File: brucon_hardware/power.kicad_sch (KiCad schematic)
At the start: 27 parts, among them J201 Conn_01x03, Q201 AO3400A, SW201 SW_SPDT, U201 TP4056, U202 MT3608, U203 HT75xx-1-SOT89

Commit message: Updated led matrix
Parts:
- renumbered C203 to C202, C204 to C203, C205 to C204, C206 to C205, C202 to C206, R209 to R201, R210 to R202, R201 to R203, R202 to R204, R204 to R205, R205 to R207, R211 to R208, R207 to R209, R208 to R210, R203 to R211
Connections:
- net VBUS: now also R201.2; no longer R201.1
- net at Q201.1 (G): now also R201.1; no longer R201.2
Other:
- moved on the sheet: R201

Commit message: Updated bom
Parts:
- C201, C203, C204: value C -> 22uF; footprint (none) -> Capacitor_SMD:C_0805_2012Metric; LCSC (none) -> C45783
- C202, C206: footprint (none) -> Capacitor_SMD:C_0805_2012Metric; LCSC (none) -> C45783
- C205: footprint (none) -> Capacitor_SMD:C_0603_1608Metric
- D201, D202: footprint (none) -> LED_SMD:LED_0805_2012Metric; LCSC (none) -> C84256
- D203: value D_Schottky -> SS54F; footprint (none) -> Diode_SMD:D_SMA; LCSC (none) -> C5359893
- J201: LCSC (none) -> C3036372
- L201: value L -> 4.7uH; footprint (none) -> Inductor_SMD:L_Sunlord_MWSA0603S; LCSC (none) -> C5307631; PNR (none) -> XR0630-4R7M
- Q201: LCSC (none) -> C20917
- R201: value R -> 10; footprint (none) -> Resistor_SMD:R_0603_1608Metric; LCSC (none) -> C22859
- R202, R203, R204: value R -> 1k; footprint (none) -> Resistor_SMD:R_0603_1608Metric; LCSC (none) -> C21190
- R205, R206, R207, R211: footprint (none) -> Resistor_SMD:R_0603_1608Metric
- R208: footprint (none) -> Resistor_SMD:R_0603_1608Metric; LCSC (none) -> C21189
- R209: value R -> 11k; footprint (none) -> Resistor_SMD:R_0603_1608Metric; LCSC (none) -> C25950
- R210: value R -> 1.5k; footprint (none) -> Resistor_SMD:R_0603_1608Metric; LCSC (none) -> C22843
- SW201: footprint (none) -> Button_Switch_SMD:SW_SPDT_PCM12; LCSC (none) -> C3036445
- U201: footprint (none) -> Package_SO:SOP-8-1EP_4.57x4.57mm_P1.27mm_EP4.57x4.45mm; LCSC (none) -> C20199357
- U202: value MT3608 -> MT3608L; LCSC (none) -> C2932326
- U203: LCSC (none) -> C499633

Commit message: Finished major parts routing led matrix
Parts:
- J201: footprint (none) -> Connector_JST:JST_SH_SM03B-SRSS-TB_1x03-1MP_P1.00mm_Horizontal
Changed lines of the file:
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@@
       (effects (font (size 1.27 1.27)) (justify left))
     )
-    (property "Footprint" "" (at 118.745 59.69 0)
+    (property "Footprint" "Connector_JST:JST_SH_SM03B-SRSS-TB_1x03-1MP_P1.00mm_Horizontal" (at 118.745 59.69 0)
       (effects (font (size 1.27 1.27)) hide)
     )

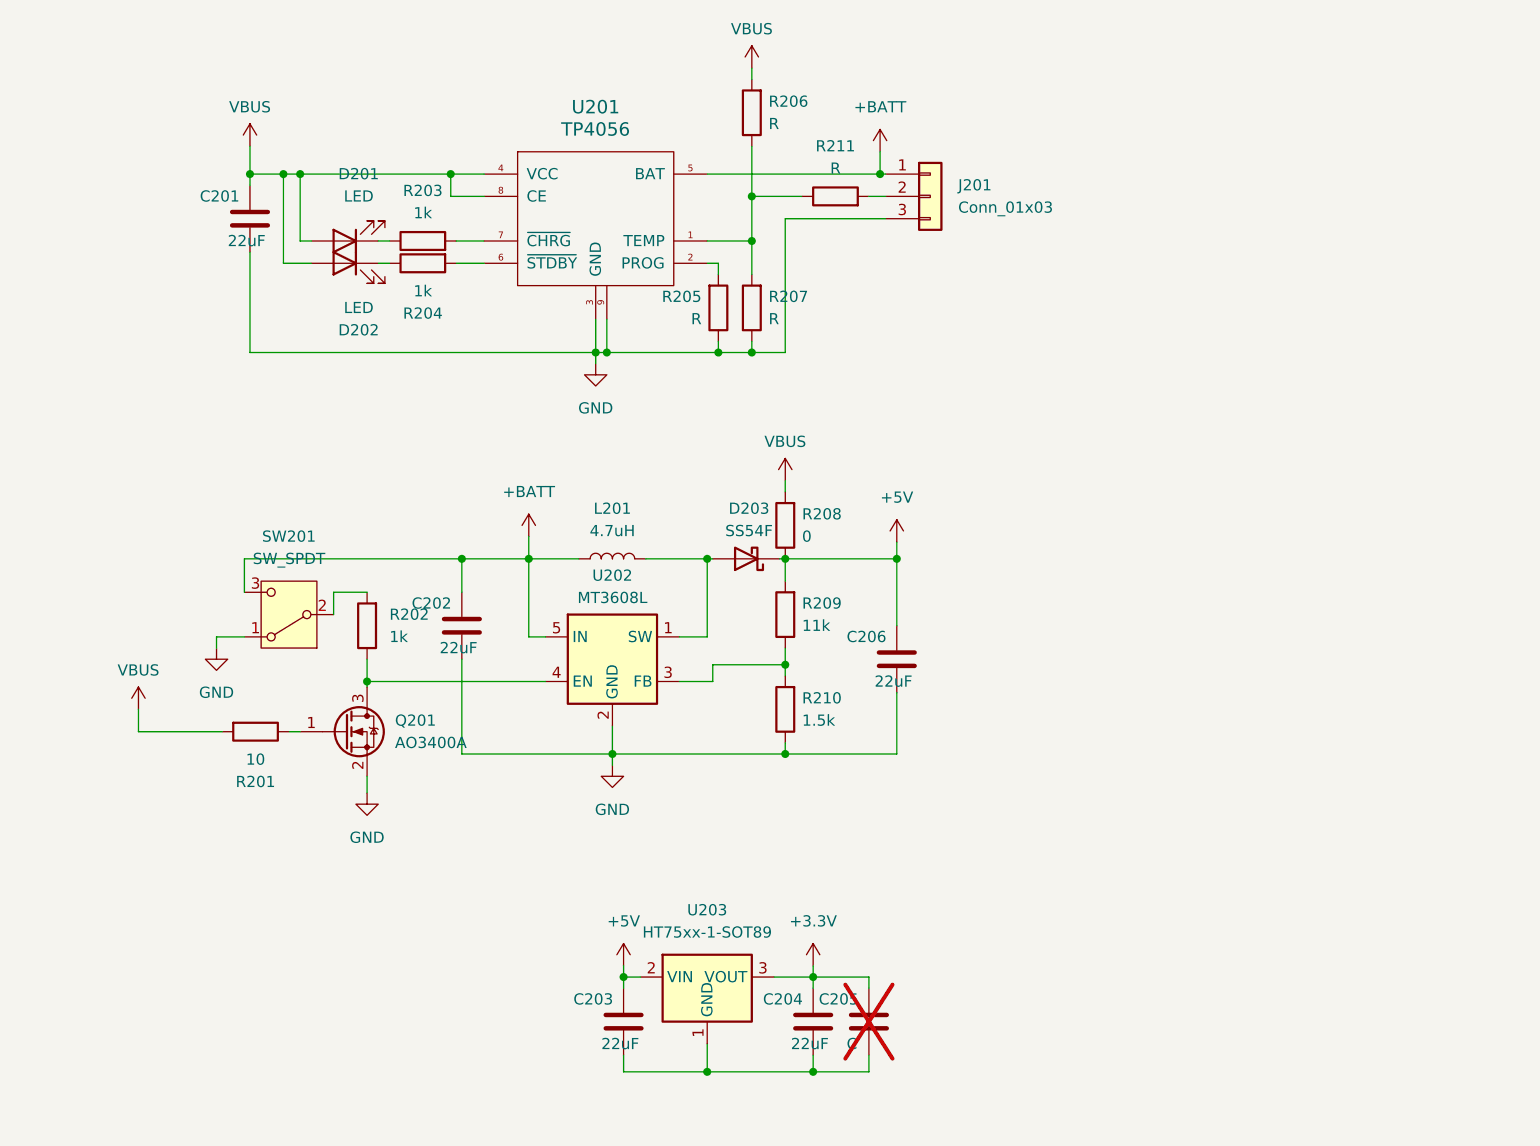
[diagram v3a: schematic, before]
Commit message: Major parts routed
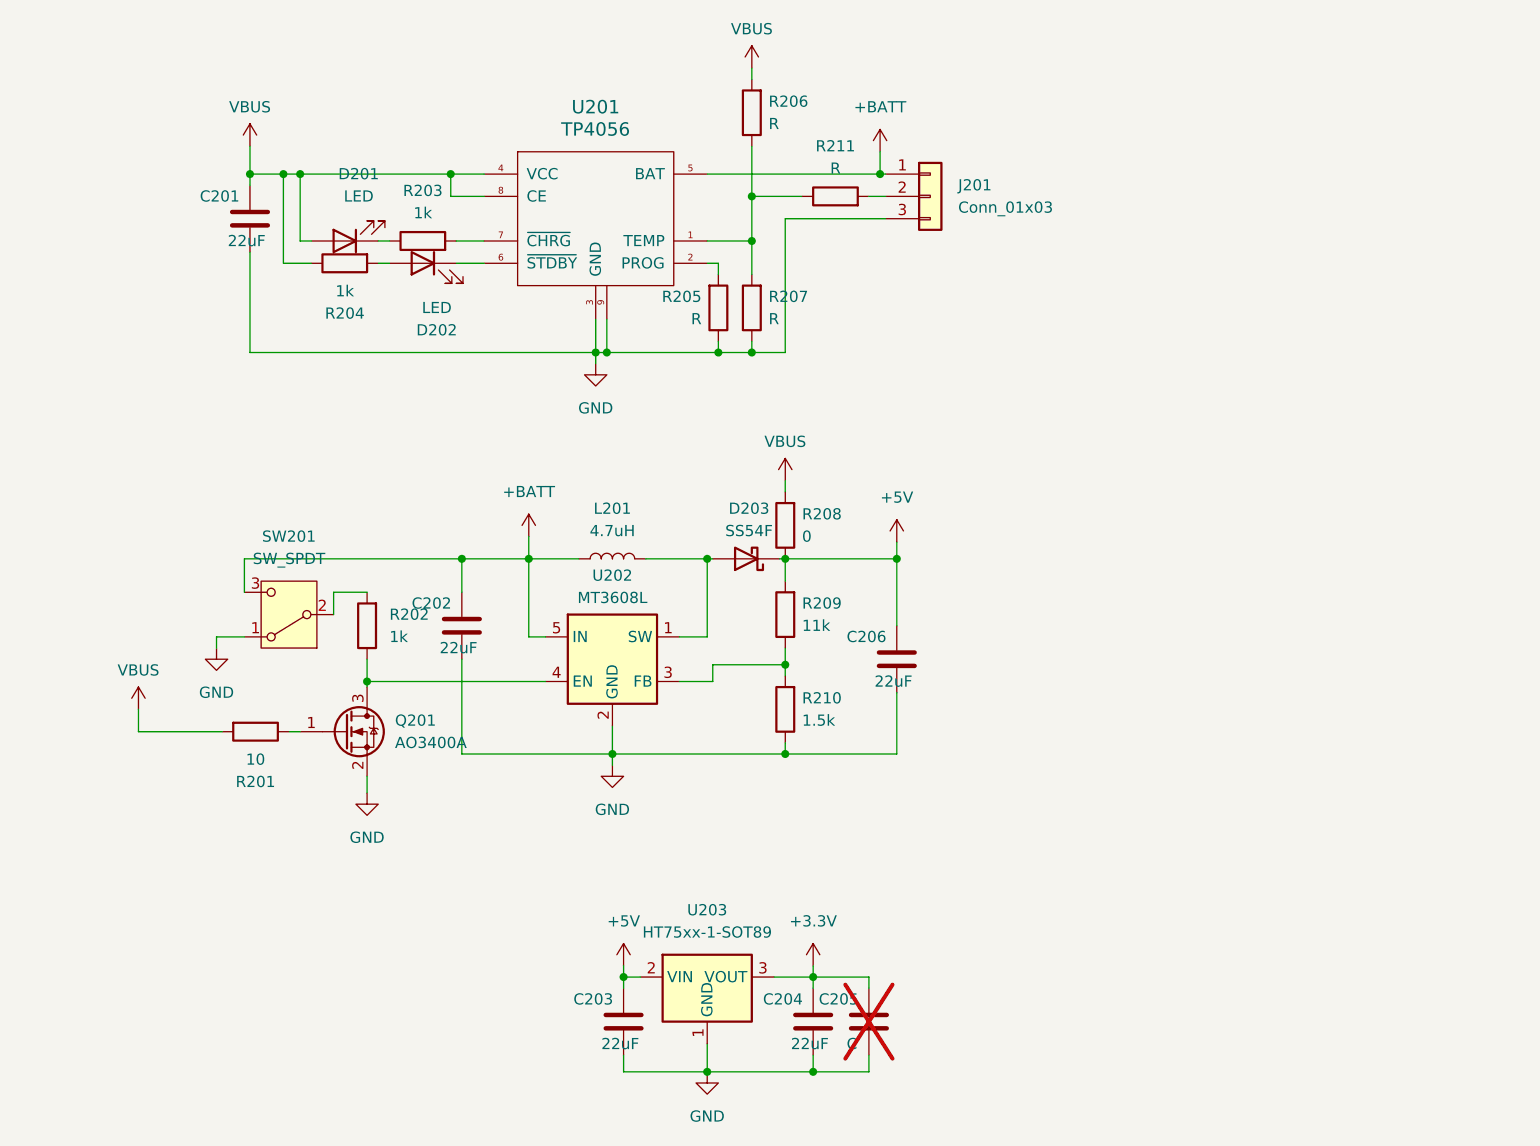
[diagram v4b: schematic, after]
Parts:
- R201, R202, R203, R204, R205, R206, R207, R208, R209, R210, R211: footprint Resistor_SMD:R_0603_1608Metric -> Resistor_SMD:R_0402_1005Metric
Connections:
- net GND: now also C203.2, C204.2, C205.2, U203.1 (GND)
- net VBUS: now also R204.1; no longer D202.2 (A)
- net at D202.1 (K): now also U201.6 (~{STDBY}); no longer R204.1
- net at R204.2: now also D202.2 (A); no longer U201.6 (~{STDBY})
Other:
- moved on the sheet: D202, R204

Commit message: As of prototype 1
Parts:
- D201, D202: value LED -> Red LED
- J201: value Conn_01x03 -> WTB01W03BB
- R205, R206, R207, R211: now not fitted
- SW201: value SW_SPDT -> AA04A02010000018A
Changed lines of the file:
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@@
 			)
 		)
-		(property "Value" "Conn_01x03"
+		(property "Value" "WTB01W03BB"
 			(at 121.92 60.96 0)
 			(effects
@@
 			)
 		)
-		(property "Datasheet" "~"
+		(property "Datasheet" "https://www.lcsc.com/datasheet/lcsc_datasheet_2207191430_BZCN-WTB01W03BB_C3036372.pdf"
 			(at 118.745 59.69 0)
 			(effects
@@
 		(in_bom yes)
 		(on_board yes)
-		(dnp no)
+		(dnp yes)
 		(fields_autoplaced yes)
 		(property "Reference" "R206"
@@
 			)
 		)
-		(property "Datasheet" "~"
+		(property "Datasheet" "https://www.lcsc.com/datasheet/lcsc_datasheet_2303131430_MSKSEMI-SS54F_C5359893.pdf"
 			(at 97.79 100.965 0)
 			(effects
@@
 			)
 		)
-		(property "Value" "SW_SPDT"
+		(property "Value" "AA04A02010000018A"
 			(at 45.72 100.965 0)
 			(effects
@@
 			)
 		)
-		(property "Datasheet" "~"
+		(property "Datasheet" "https://www.lcsc.com/datasheet/lcsc_datasheet_2207121430_BZCN-AA04A02010000018A_C3036445.pdf"
 			(at 45.72 99.695 0)
 			(effects
@@
 		(in_bom yes)
 		(on_board yes)
-		(dnp no)
+		(dnp yes)
 		(property "Reference" "R205"
 			(at 92.71 71.12 0)
@@
 			)
 		)
-		(property "Value" "LED"
+		(property "Value" "Red LED"
 			(at 53.6575 59.69 0)
 			(effects
@@
 			)
 		)
-		(property "Datasheet" "~"
+		(property "Datasheet" "https://www.lcsc.com/datasheet/lcsc_datasheet_2304140030_Foshan-NationStar-Optoelectronics-NCD0805R1_C84256.pdf"
 			(at 52.07 64.77 0)
 			(effects
@@
 			)
 		)
-		(property "Datasheet" ""
+		(property "Datasheet" "https://www.lcsc.com/datasheet/lcsc_datasheet_2312291747_YONGYUTAI-TP4056_C20199357.pdf"
 			(at 80.645 63.5 0)
 			(effects
@@
 			)
 		)
-		(property "Datasheet" "~"
+		(property "Datasheet" "https://www.lcsc.com/datasheet/lcsc_datasheet_2403281214_XR-XR0630-4R7M_C5307631.pdf"
 			(at 82.55 100.965 0)
 			(effects
@@
 		(in_bom yes)
 		(on_board yes)
-		(dnp no)
+		(dnp yes)
 		(fields_autoplaced yes)
 		(property "Reference" "R211"
@@
 		(in_bom yes)
 		(on_board yes)
-		(dnp no)
+		(dnp yes)
 		(fields_autoplaced yes)
 		(property "Reference" "R207"
@@
 			)
 		)
-		(property "Value" "LED"
+		(property "Value" "Red LED"
 			(at 62.5475 72.39 0)
 			(effects
@@
 			)
 		)
-		(property "Datasheet" "~"
+		(property "Datasheet" "https://www.lcsc.com/datasheet/lcsc_datasheet_2304140030_Foshan-NationStar-Optoelectronics-NCD0805R1_C84256.pdf"
 			(at 60.96 67.31 0)
 			(effects

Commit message: Updated hardware
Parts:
- removed D203: SS54F, Diode_SMD:D_SMA, symbol Device:D_Schottky
- removed Q201: AO3400A, Package_TO_SOT_SMD:SOT-23, symbol Transistor_FET:AO3400A
- removed R201: 10, Resistor_SMD:R_0402_1005Metric, symbol Device:R
- removed R202: 1k, Resistor_SMD:R_0402_1005Metric, symbol Device:R
- removed R205, R206, R207, R211: R, Resistor_SMD:R_0402_1005Metric, symbol Device:R
- removed R208: 0, Resistor_SMD:R_0402_1005Metric, symbol Device:R
- removed R209: 11k, Resistor_SMD:R_0402_1005Metric, symbol Device:R
- removed R210: 1.5k, Resistor_SMD:R_0402_1005Metric, symbol Device:R
- removed SW201: AA04A02010000018A, Button_Switch_SMD:SW_SPDT_PCM12, symbol Switch:SW_SPDT
- removed U201: TP4056, Package_SO:SOP-8-1EP_4.57x4.57mm_P1.27mm_EP4.57x4.45mm, symbol tp4056:TP4056
- removed U202: MT3608L, Package_TO_SOT_SMD:SOT-23-6, symbol Regulator_Switching:MT3608
- added C1, C2, C3: 10uF, Capacitor_SMD:C_0603_1608Metric, symbol Device:C
- added C7: 22uF, Capacitor_SMD:C_0805_2012Metric, symbol Device:C
- added Q1: AO3400A, Package_TO_SOT_SMD:SOT-23, symbol Transistor_FET:AO3400A
- added R1: 2, Resistor_SMD:R_0402_1005Metric, symbol Device:R
- added R2: 10k, Resistor_SMD:R_0402_1005Metric, symbol Device:R
- added U1: IP5306, Package_SO:HSOP-8-1EP_3.9x4.9mm_P1.27mm_EP2.41x3.1mm_ThermalVias, symbol IP5306:IP5306
- C201: now not fitted
- L201: value 4.7uH -> 2.2uH; footprint Inductor_SMD:L_Sunlord_MWSA0603S -> Inductor_SMD:L_Changjiang_FNR5030S; LCSC C5307631 -> C7588710; PNR XR0630-4R7M -> (none)
- R203, R204: value 1k -> 0; LCSC C21190 -> (none)
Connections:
- net +5V: now also C201.1, C202.1, C7.1, U1.8 (VOUT)
- net +BATT: now also J201.3 (Pin_3), L201.2, C3.1, U1.3 (LED2), U1.6 (BAT); no longer C202.1, J201.1 (Pin_1), L201.1
- net GND: now also D201.1 (K), D202.1 (K), J201.1 (Pin_1), C1.2, C2.2, C3.2, C7.2, Q1.2 (S), U1.9 (EP); no longer J201.3 (Pin_3)
- net VBUS: now also C2.1, R1.2, U1.1 (VIN); no longer C201.1, D201.2 (A), R204.1
- net at R204.2: now also U1.4 (LED3); no longer D202.2 (A)
- net at R203.1: now also D202.2 (A); no longer D201.1 (K)
- net at R203.2: now also U1.2 (LED1)
- new net: D201.2 (A), R204.1
- new net: R2.2, U1.5 (KEY)
- new net: L201.1, U1.7 (SW)
- new net: Q1.3 (D), R2.1
- new net: C1.1, R1.1
- new net ENABLE: Q1.1 (G)
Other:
- moved on the sheet: C202, C203, C204, C205, C206, D201, D202, J201, L201, R203, R204, U203

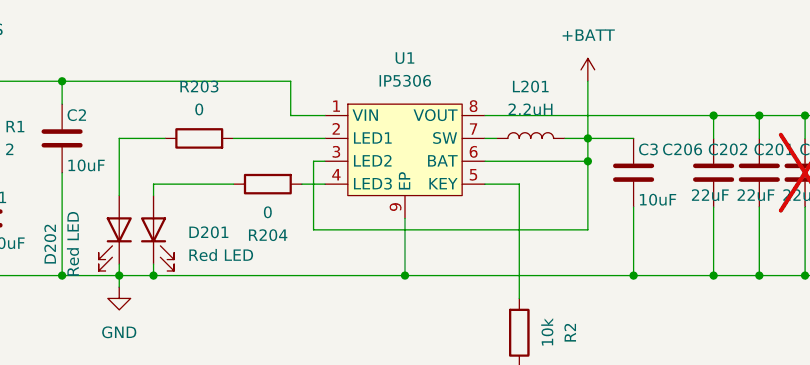
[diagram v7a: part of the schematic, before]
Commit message: Updated part numbers
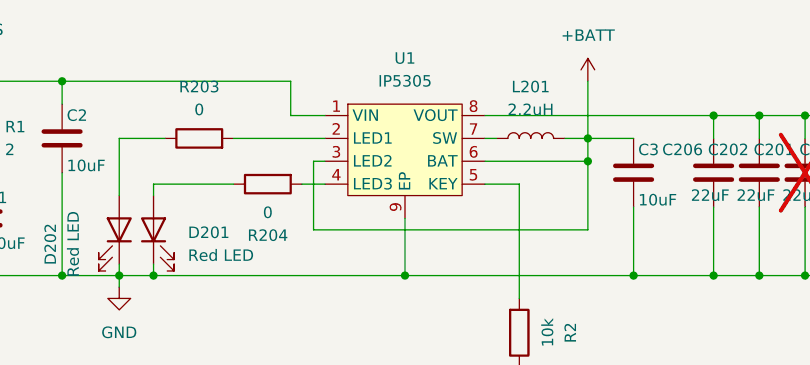
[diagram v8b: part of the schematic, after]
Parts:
- C1, C2, C3: LCSC (none) -> C6119842
- Q1: LCSC (none) -> C347475
- R1: LCSC (none) -> C22977
- R2: LCSC (none) -> C25804
- R203, R204: LCSC (none) -> C21189
- U1: value IP5306 -> IP5305; LCSC (none) -> C181686
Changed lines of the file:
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@@
 			)
 		)
-		(property "LCSC" ""
+		(property "LCSC" "C21189"
 			(at 83.82 74.93 0)
 			(effects
@@
 			)
 		)
-		(property "Value" "IP5306"
+		(property "Value" "IP5305"
 			(at 99.06 63.5 0)
 			(effects
@@
 		)
 		(property "Description" ""
+			(at 99.06 69.85 0)
+			(effects
+				(font
+					(size 1.27 1.27)
+				)
+				(hide yes)
+			)
+		)
+		(property "LCSC" "C181686"
 			(at 99.06 69.85 0)
 			(effects
@@
 			)
 		)
+		(property "LCSC" "C347475"
+			(at 109.22 101.6 0)
+			(effects
+				(font
+					(size 1.27 1.27)
+				)
+				(hide yes)
+			)
+		)
 		(pin "3"
 		)
@@
 			)
 		)
-		(property "LCSC" ""
+		(property "LCSC" "C22977"
 			(at 52.07 69.85 0)
 			(effects
@@
 		)
 		(property "Description" "Unpolarized capacitor"
+			(at 124.46 73.66 0)
+			(effects
+				(font
+					(size 1.27 1.27)
+				)
+				(hide yes)
+			)
+		)
+		(property "LCSC" "C6119842"
 			(at 124.46 73.66 0)
 			(effects
@@
 			)
 		)
-		(property "LCSC" ""
+		(property "LCSC" "C25804"
 			(at 111.76 91.44 0)
 			(effects
@@
 			)
 		)
-		(property "LCSC" ""
+		(property "LCSC" "C21189"
 			(at 76.2 69.85 0)
 			(effects
@@
 		)
 		(property "Description" "Unpolarized capacitor"
+			(at 60.96 69.85 0)
+			(effects
+				(font
+					(size 1.27 1.27)
+				)
+				(hide yes)
+			)
+		)
+		(property "LCSC" "C6119842"
 			(at 60.96 69.85 0)
 			(effects
@@
 			(at 52.07 78.74 0)
 			(effects
+				(font
+					(size 1.27 1.27)
+				)
+				(hide yes)
+			)
+		)
+		(property "LCSC" "C6119842"
+			(at 52.07 78.74 0)
+			(effects
